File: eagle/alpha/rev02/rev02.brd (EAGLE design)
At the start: 100 x 80 mm, 381 parts, among them CN1 HOST, CN2 HOST, IC1 N25Q128A13ES, IC2 74AC244DW, IC3 N25Q128A13ES, J1 STM32-SWD, Q1 2N7002, Q2 BC818, Q4 2N7002, Q5 ASFL1, Q6 2N7002, T1 BC847, T2 BC847, U1 LMZ13608, U10 ATTINY828R-AU, U11 MC14551BDG, U12 23K640-I/SN, U13 XC7A200TFBG484, U14 EN6347QI, U15 EN6347QI, U16 EN5364QI, U2 LT3060ITS8-15, U3 MC74HC1G14DTT1G, U4 STM32F429BIT6, U5 IS45S32160F, U6 IS45S32160F, U7 MCP79412-I/SN, U8 FT232H_SERIAL, U9 FT232H_SERIAL, Y1 12 MHz, Y2 12 MHz

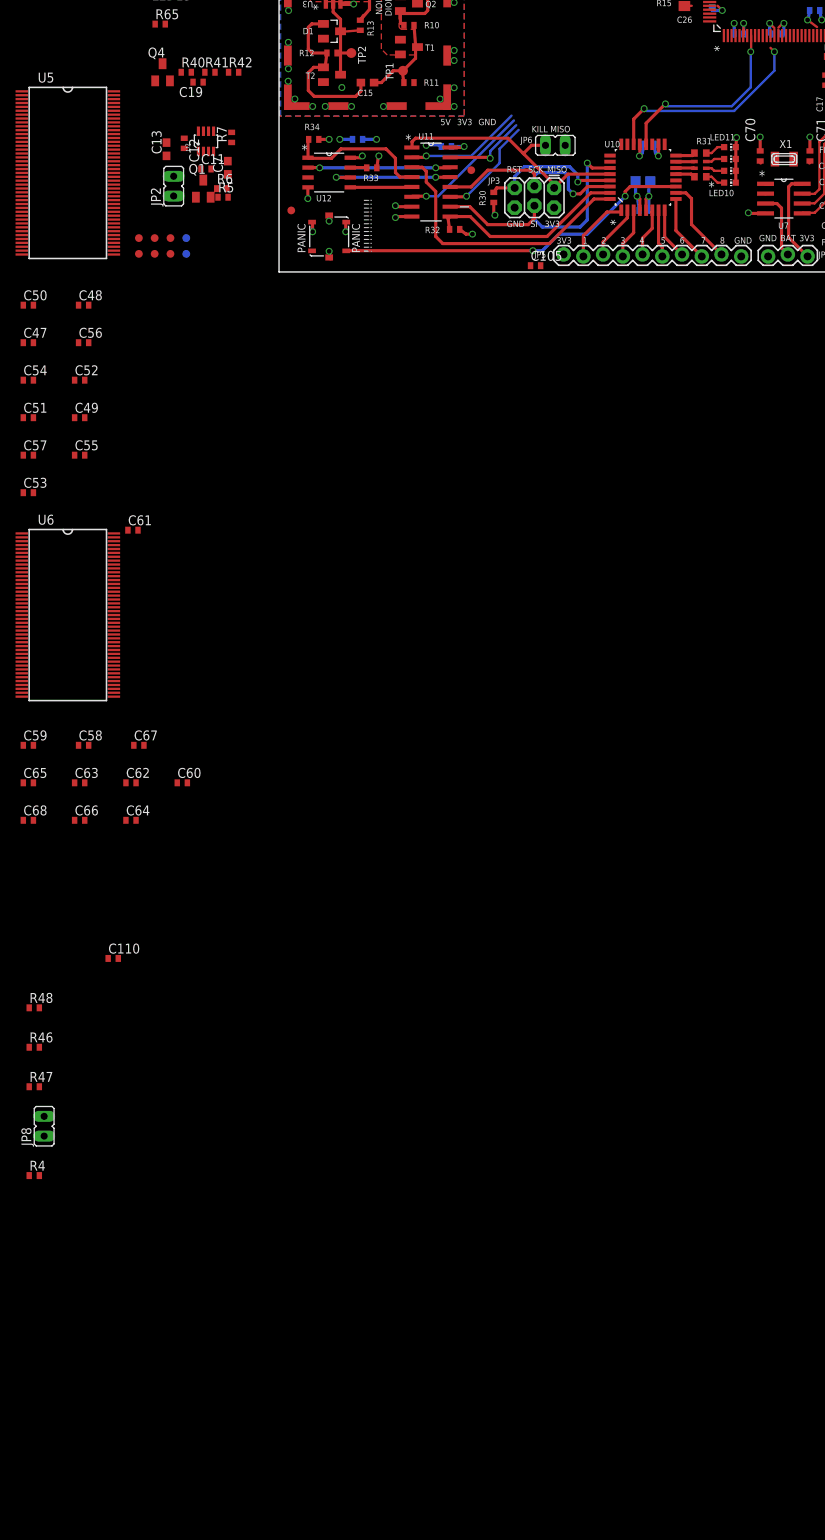
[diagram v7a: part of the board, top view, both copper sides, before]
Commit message: More schematic updates after review with Pavel.
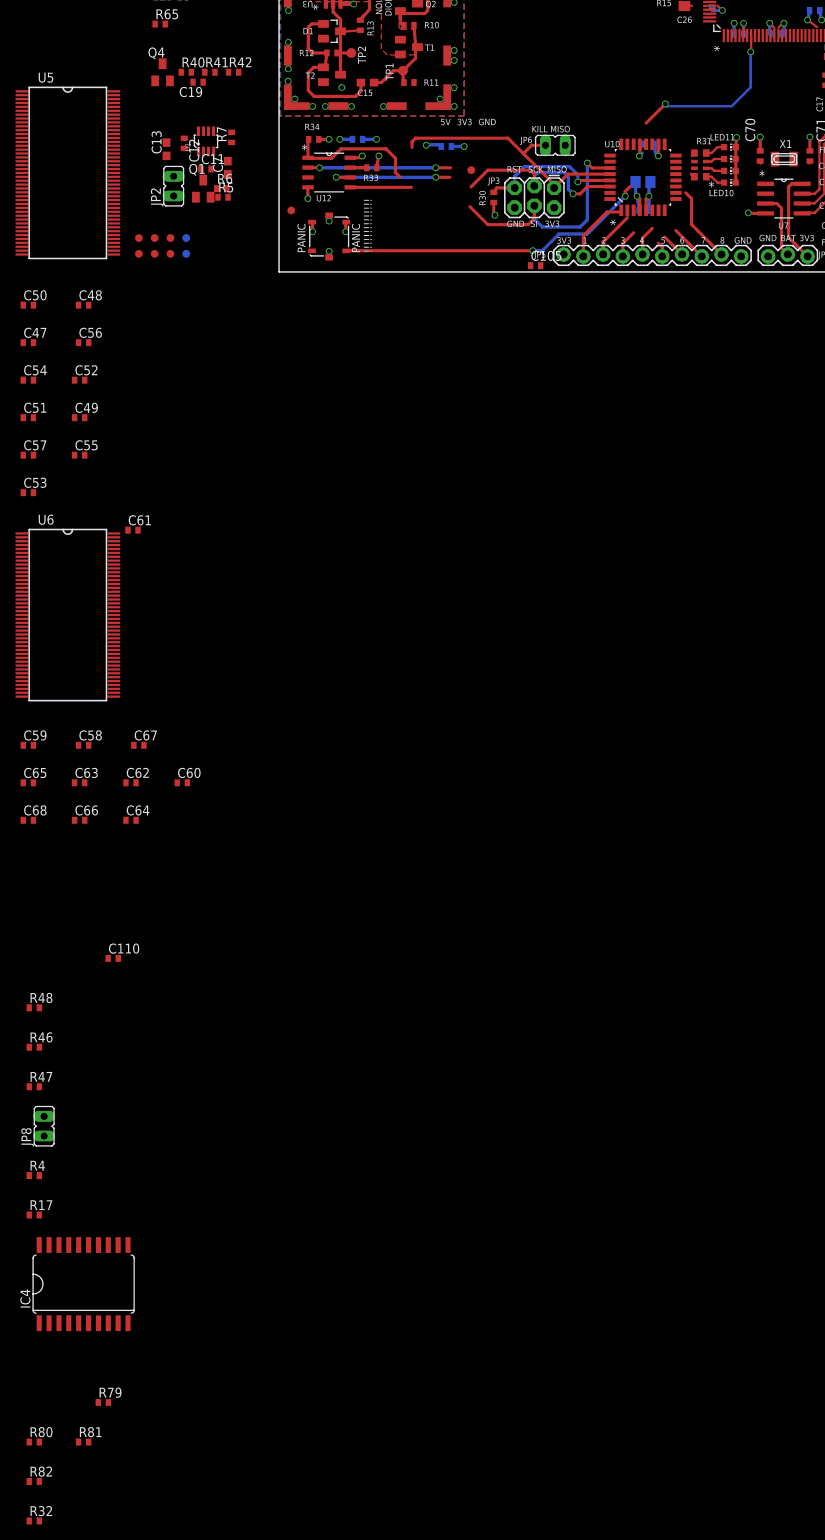
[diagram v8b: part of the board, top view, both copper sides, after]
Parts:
- removed U11: MC14551BDG, ON_Semiconductor-MC14551BDG:SOIC127P600X175-16N
- added IC4: 74AC244DW, 74xx-eu:SO20W
- added R17, R79, R80, R81: 4.7k, resistor:R0402
- added R82: 15k, resistor:R0402
- R32: value 15k -> 0
- R33, R34: value 15k -> 4.7k
- moved R32 174.8 mm to (-11.4, -160.0), turned to 0 degrees
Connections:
- removed net AVR_GPIO_10: U10.20, U4.8
- removed net AVR_GPIO_11: U10.22, U4.9
- removed net AVR_GPIO_8: JP5.9, U10.10
- removed net FPGA_GPIO_TAMPER_0: U10.25, U13.F15
- removed net FPGA_GPIO_TAMPER_1: U10.26, U13.F13
- removed net MKM_CONTROL: R32.2, U10.31, U11.9
- removed net SDIO_CK: U4.163
- removed net SDIO_CMD: U4.166
- removed net SDIO_D0: U4.140
- removed net SDIO_D1: U4.141
- removed net SDIO_D2: U4.161
- removed net SDIO_D3: U4.162
- new net AVR_GPIO_0: JP5.2, U10.31
- new net AVR_GPIO_ARM_0: U10.17, U4.8
- new net AVR_GPIO_ARM_1: U10.19, U4.9
- new net AVR_GPIO_FPGA_2: U10.25
- new net AVR_GPIO_FPGA_3: U10.26
- new net MKM_CONTROL_AVR_ENA: IC4.1, R80.1, U10.15
- new net MKM_CONTROL_FPGA_DIS: IC4.19, R81.1
- new net N$23: IC1.3, R17.2
- new net N$25: U4.6
- new net N$53: R32.2
- net 3V3_BATT: now also IC4.20, R32.1, R79.2, R80.2, R82.2; no longer U11.16
- net AVR_GPIO_1: now also JP5.3, U10.32; no longer JP5.2, U10.1
- net AVR_GPIO_2: now also JP5.4, U10.1; no longer JP5.3, U10.2
- net AVR_GPIO_3: now also JP5.5, U10.2; no longer JP5.4, U10.3
- net AVR_GPIO_4: now also JP5.6, U10.3; no longer JP5.5, U10.6
- net AVR_GPIO_5: now also JP5.7, U10.6; no longer JP5.6, U10.7
- net AVR_GPIO_6: now also JP5.8, U10.7; no longer JP5.7, U10.8
- net AVR_GPIO_7: now also JP5.9, U10.8; no longer JP5.8, U10.9
- net AVR_LED1: now also U10.9; no longer U10.16
- net AVR_LED2: now also U10.10; no longer U10.15
- net AVR_LED3: now also U10.11; no longer U10.14
- net AVR_LED4: now also U10.12; no longer U10.13
- net AVR_PANIC: now also R82.1; no longer U10.11
- net GND: now also IC4.10, R81.2; no longer R32.1, U11.7, U11.8
- net MKM_AVR_CS_N: now also IC4.2, U10.14; no longer U10.32, U11.3
- net MKM_AVR_MISO: now also IC4.12; no longer U11.1
- net MKM_AVR_MOSI: now also IC4.6; no longer U11.10
- net MKM_AVR_SCK: now also IC4.4; no longer U11.12
- net MKM_CS_N: now also IC4.18, IC4.9, R79.1; no longer U11.4
- net MKM_FPGA_CS_N: now also IC4.11; no longer U11.2
- net MKM_FPGA_MISO: now also IC4.3; no longer U11.15
- net MKM_FPGA_MOSI: now also IC4.15; no longer U11.6
- net MKM_FPGA_SCK: now also IC4.13; no longer U11.11
- net MKM_MISO: now also IC4.17, IC4.8; no longer U11.14
- net MKM_MOSI: now also IC4.14, IC4.5; no longer U11.5
- net MKM_SCK: now also IC4.16, IC4.7; no longer U11.13
- net VCCO_3V3: now also R17.1; no longer IC1.3, U4.6
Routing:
- net MKM_AVR_CS_N: track 36.1 -> 0.00 mm
- net AVR_GPIO_11: track 27.7 -> 0.00 mm, vias 2 -> 0
- net MKM_CONTROL: track 25.7 -> 0.00 mm
- net AVR_GPIO_10: track 25.2 -> 0.00 mm, vias 2 -> 0
- net AVR_GPIO_ARM_0: track 0.00 -> 22.5 mm, vias 0 -> 2
- net MKM_FPGA_MOSI: track 17.2 -> 0.00 mm, vias 1 -> 0
- net MKM_FPGA_CS_N: track 15.0 -> 0.00 mm, vias 1 -> 0
- net MKM_FPGA_SCK: track 13.9 -> 0.00 mm, vias 1 -> 0
- net AVR_GPIO_8: track 11.1 -> 0.00 mm
- net MKM_FPGA_MISO: track 10.9 -> 0.00 mm, vias 1 -> 0
- net AVR_GPIO_0: track 0.00 -> 8.81 mm
- net GND: track 140.6 -> 133.3 mm, vias 59 -> 56
- net AVR_PANIC: track 46.3 -> 40.4 mm
- net AVR_GPIO_4: track 6.21 -> 1.90 mm
- net AVR_GPIO_2: track 6.98 -> 3.63 mm
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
